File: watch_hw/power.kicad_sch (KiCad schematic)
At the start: 21 parts, among them Q2 SSM6J501NU, U3 MAX17048G+, U4 LTC3130EUDC-1#PBF, U5 MCP73831-2ACI{slash}MC

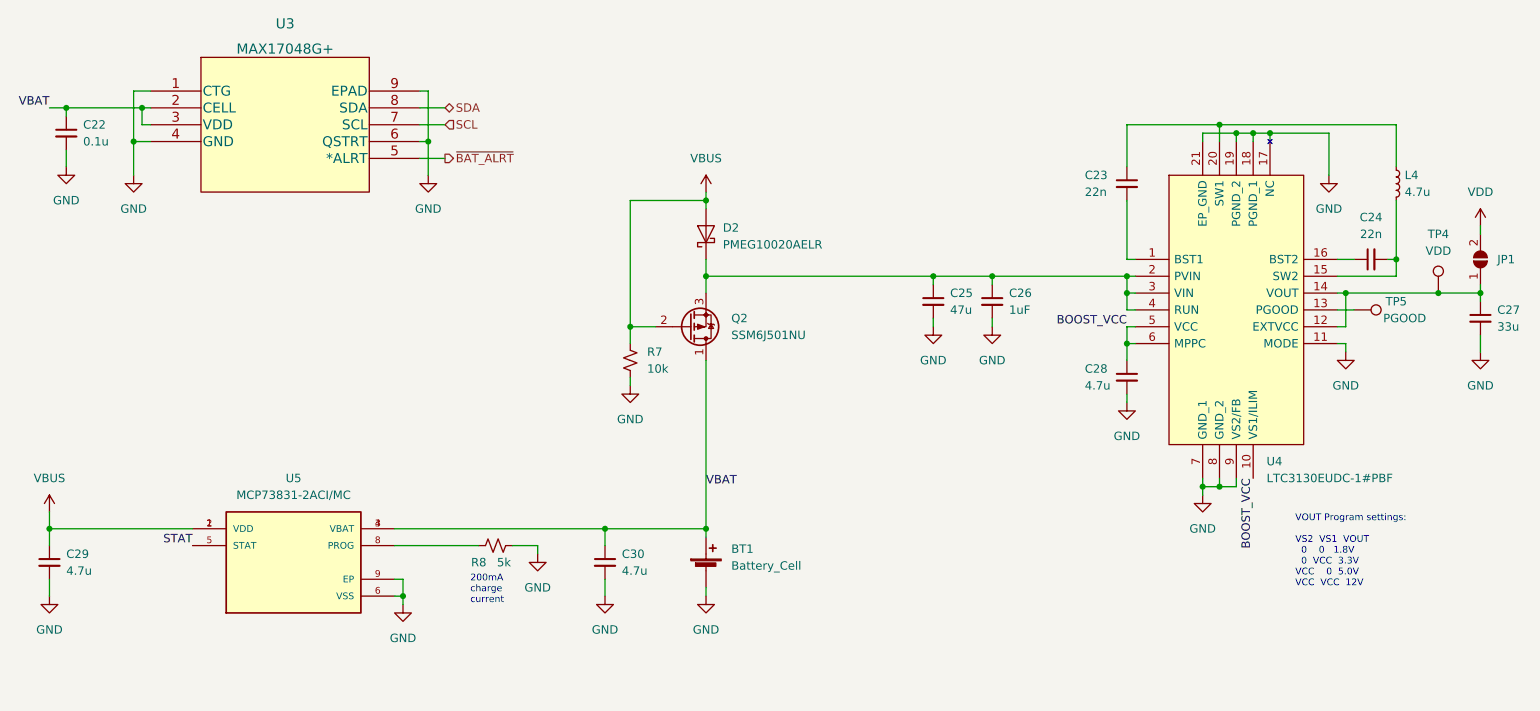
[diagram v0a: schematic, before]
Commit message: Finalize (?) part selection, start layout
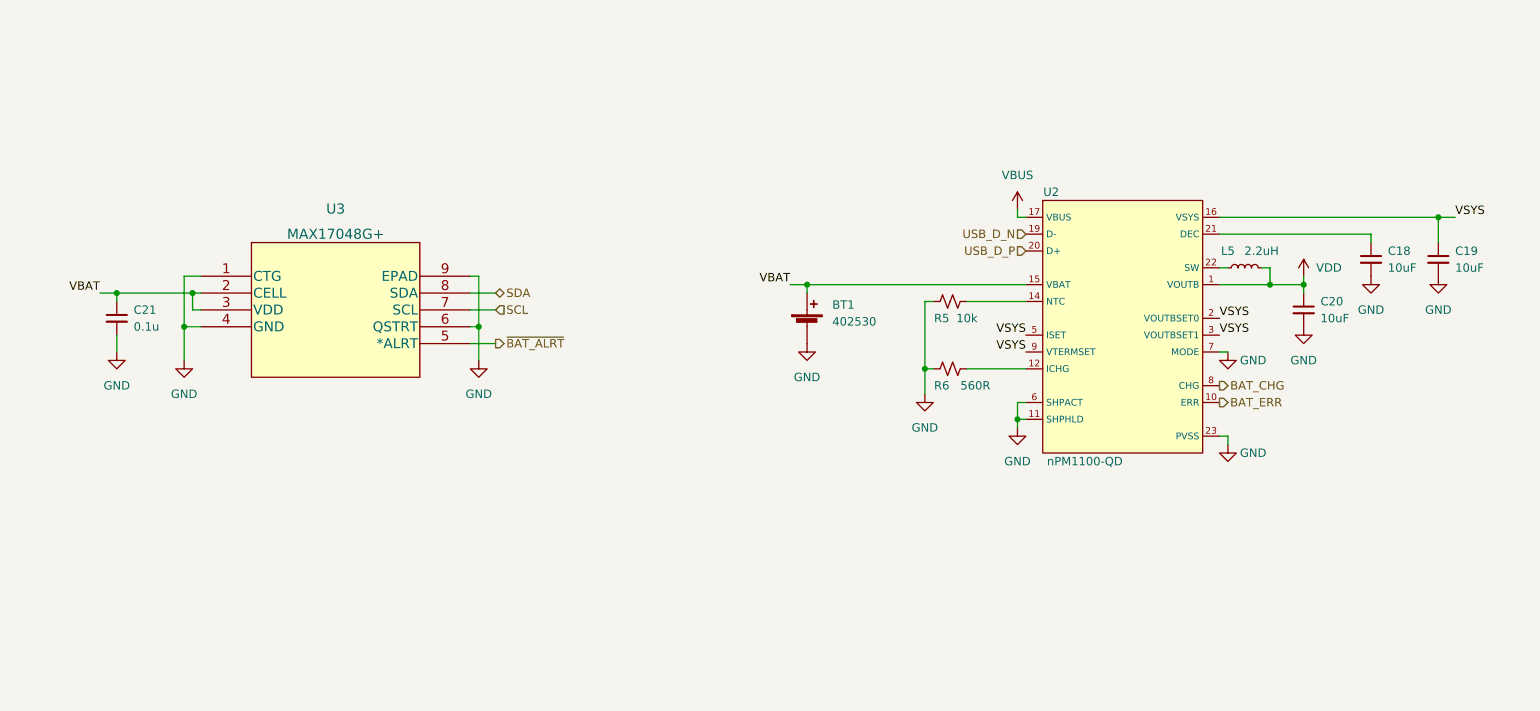
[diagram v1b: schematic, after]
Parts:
- removed C23, C24: 22n, Capacitor_SMD:C_0402_1005Metric_Pad0.74x0.62mm_HandSolder, symbol Device:C_Small
- removed C25: 47u, Capacitor_SMD:C_0402_1005Metric_Pad0.74x0.62mm_HandSolder, symbol Device:C_Small
- removed C26: 1uF, Capacitor_SMD:C_0402_1005Metric_Pad0.74x0.62mm_HandSolder, symbol Device:C_Small
- removed C27: 33u, Capacitor_SMD:C_0402_1005Metric_Pad0.74x0.62mm_HandSolder, symbol Device:C_Small
- removed C28, C29, C30: 4.7u, Capacitor_SMD:C_0402_1005Metric_Pad0.74x0.62mm_HandSolder, symbol Device:C_Small
- removed D2: PMEG10020AELR, Diode_SMD:Nexperia_CFP3_SOD-123W, symbol Diode:PMEG10020AELR
- removed JP1: SolderJumper_2_Open, Jumper:SolderJumper-2_P1.3mm_Open_RoundedPad1.0x1.5mm, symbol Jumper:SolderJumper_2_Open
- removed L4: 4.7u, Inductor_SMD:L_0805_2012Metric_Pad1.15x1.40mm_HandSolder, symbol Device:L_Small
- removed Q2: SSM6J501NU, watch:TRANS_SSM6J501NU,LF, symbol Device:Q_PMOS_DGS
- removed R7: 10k, Resistor_SMD:R_0402_1005Metric_Pad0.72x0.64mm_HandSolder, symbol Device:R_Small_US
- removed R8: 5k, Resistor_SMD:R_0402_1005Metric_Pad0.72x0.64mm_HandSolder, symbol Device:R_Small_US
- removed TP4: VDD, TestPoint:TestPoint_THTPad_D1.0mm_Drill0.5mm, symbol Connector:TestPoint
- removed TP5: PGOOD, TestPoint:TestPoint_THTPad_D1.0mm_Drill0.5mm, symbol Connector:TestPoint
- removed U4: LTC3130EUDC-1#PBF, watch:QFN50P300X400X80-21M-D, symbol watch:LTC3130EUDC-1#PBF
- removed U5: MCP73831-2ACI/MC, watch:SON50P200X300X100-9N, symbol watch:MCP73831-2ACI{brace}slash}MC
- added C18, C19, C20: 10uF, Capacitor_SMD:C_0805_2012Metric_Pad1.18x1.45mm_HandSolder, symbol Device:C_Small
- added L5: 2.2uH, Inductor_SMD:L_0805_2012Metric_Pad1.05x1.20mm_HandSolder, symbol Device:L_Small
- added R5: 10k, Resistor_SMD:R_0402_1005Metric_Pad0.72x0.64mm_HandSolder, symbol Device:R_Small_US
- added R6: 560R, Resistor_SMD:R_0402_1005Metric_Pad0.72x0.64mm_HandSolder, symbol Device:R_Small_US
- added U2: nPM1100-QD, watch:nPM1100-QD, symbol watch:nPM1100-QD
- BT1: value Battery_Cell -> 402530
- renumbered C22 to C21
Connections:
- net GND: now also C18.2, C19.2, C20.2, R5.1, R6.1, U2.11 (SHPHLD), U2.23 (PVSS), U2.6 (SHPACT), U2.7 (MODE)
- net VBAT: now also U2.15 (VBAT)
- net VBUS: now also U2.17 (VBUS)
- net VDD: now also C20.1, L5.2, U2.1 (VOUTB)
- new net: L5.1, U2.22 (SW)
- new net: C18.1, U2.21 (DEC)
- new net: R5.2, U2.14 (NTC)
- new net: R6.2, U2.12 (ICHG)
- new net BAT_CHG: U2.8 (CHG)
- new net BAT_ERR: U2.10 (ERR)
- new net USB_D_N: U2.19 (D-)
- new net USB_D_P: U2.20 (D+)
- new net VSYS: C19.1, U2.16 (VSYS), U2.2 (VOUTBSET0), U2.3 (VOUTBSET1), U2.5 (ISET), U2.9 (VTERMSET)
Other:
- note removed: "200mA charge current"
- note removed: "VOUT Program settings: VS2 VS1 VOUT 0 0 1.8V 0 VCC 3.3V VCC 0 5.0V VCC VCC 12V"
- moved on the sheet: BT1, C21, U3

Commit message: Clean up library symbols, update to kicad 8
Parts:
- C21: value 0.1u -> 0.1uF

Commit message: Start watch v1 layout
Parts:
- added TP1, TP2, TP3, TP4: TestPoint, TestPoint:TestPoint_Keystone_5015_Micro_Mini, symbol Connector:TestPoint
- U2: footprint watch:nPM1100-QD -> Package_DFN_QFN:QFN-24-1EP_4x4mm_P0.5mm_EP2.5x2.5mm
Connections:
- net GND: now also TP1.1
- net VBAT: now also TP3.1
- net VDD: now also TP2.1
- net VSYS: now also TP4.1

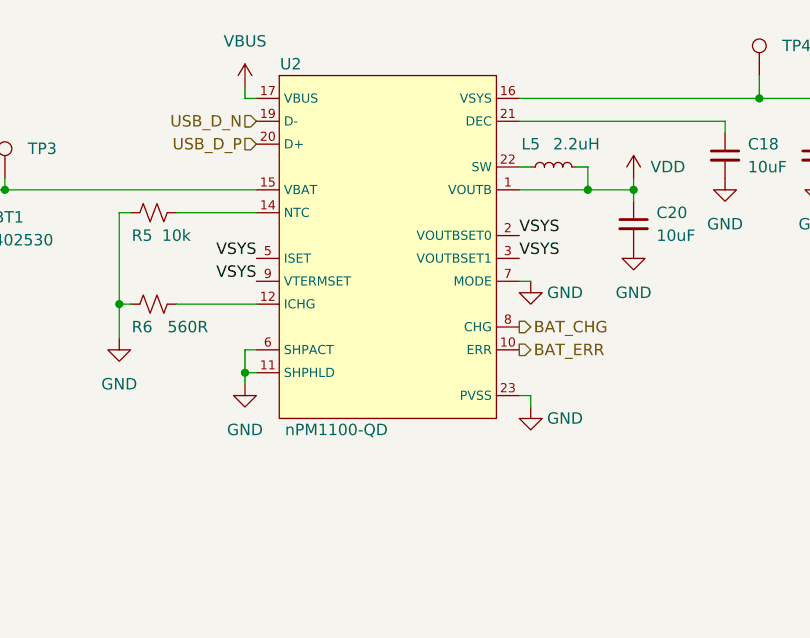
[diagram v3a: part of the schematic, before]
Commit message: Add pulse sensor straight to board, fix NPM1100 symbol/footprint
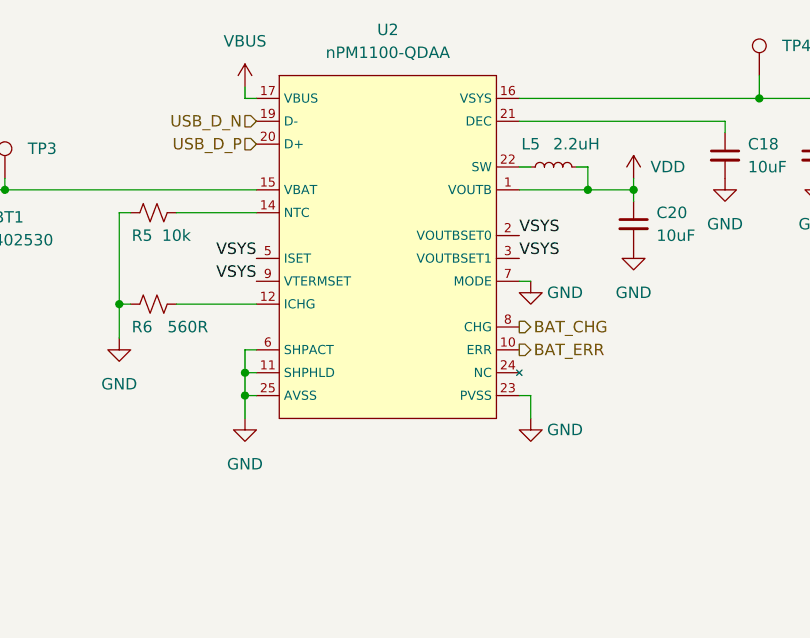
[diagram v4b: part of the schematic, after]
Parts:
- removed U2: nPM1100-QD, Package_DFN_QFN:QFN-24-1EP_4x4mm_P0.5mm_EP2.5x2.5mm, symbol watch:nPM1100-QD
- added U2: nPM1100-QDAA, Package_DFN_QFN:QFN-24-1EP_4x4mm_P0.5mm_EP2.15x2.15mm, symbol watch:nPM1100-QDAA
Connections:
- net BAT_CHG: now also U2.8 (CHG)
- net BAT_ERR: now also U2.10 (ERR)
- net GND: now also U2.11 (SHPHLD), U2.23 (PVSS), U2.25 (AVSS), U2.6 (SHPACT), U2.7 (MODE)
- net USB_D_N: now also U2.19 (D-)
- net USB_D_P: now also U2.20 (D+)
- net VBAT: now also U2.15 (VBAT)
- net VBUS: now also U2.17 (VBUS)
- net VDD: now also U2.1 (VOUTB)
- net VSYS: now also U2.16 (VSYS), U2.2 (VOUTBSET0), U2.3 (VOUTBSET1), U2.5 (ISET), U2.9 (VTERMSET)
- net at L5.1: now also U2.22 (SW)
- net at C18.1: now also U2.21 (DEC)
- net at R5.2: now also U2.14 (NTC)
- net at R6.2: now also U2.12 (ICHG)
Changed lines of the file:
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@@
+	)
+	(junction
+		(at 185.42 106.68)
+		(diameter 0)
+		(color 0 0 0 0)
 	)
 	(junction
@@
 	(wire
 		(pts
+			(xy 185.42 106.68) (xy 186.69 106.68)
+		)
+		(stroke
+			(width 0)
+			(type default)
+		)
+	)
+	(wire
+		(pts
 			(xy 158.75 83.82) (xy 186.69 83.82)
 		)
@@
 	(wire
 		(pts
-			(xy 185.42 105.41) (xy 185.42 104.14)
+			(xy 185.42 109.22) (xy 185.42 106.68)
 		)
 		(stroke
@@
 	(wire
 		(pts
+			(xy 185.42 106.68) (xy 185.42 104.14)
+		)
+		(stroke
+			(width 0)
+			(type default)
+		)
+	)
+	(wire
+		(pts
 			(xy 185.42 72.39) (xy 185.42 73.66)
 		)
@@
 	(wire
 		(pts
-			(xy 217.17 107.95) (xy 217.17 106.68)
+			(xy 217.17 109.22) (xy 217.17 106.68)
 		)
 		(stroke
@@
 	)
 	(symbol
+		(lib_id "watch:nPM1100-QDAA")
+		(at 186.69 73.66 0)
+		(unit 1)
+		(exclude_from_sim no)
+		(in_bom yes)
+		(on_board yes)
+		(dnp no)
+		(fields_autoplaced yes)
+		(property "Reference" "U2"
+			(at 201.295 66.04 0)
+			(effects
+				(font
+					(size 1.27 1.27)
+				)
+			)
+		)
+		(property "Value" "nPM1100-QDAA"
+			(at 201.295 68.58 0)
+			(effects
+				(font
+					(size 1.27 1.27)
+				)
+			)
+		)
+		(property "Footprint" "Package_DFN_QFN:QFN-24-1EP_4x4mm_P0.5mm_EP2.15x2.15mm"
+			(at 199.39 64.77 0)
+			(effects
+				(font
+					(size 1.27 1.27)
+				)
+				(hide yes)
+			)
+		)
+		(property "Datasheet" "https://infocenter.nordicsemi.com/pdf/nPM1100_PS_v1.3.pdf"
+			(at 187.96 73.66 0)
+			(effects
+				(font
+					(size 1.27 1.27)
+				)
+				(hide yes)
+			)
+		)
+		(property "Description" "POWER MANAGEMENT IC QFN24 VTERM"
+			(at 186.69 73.66 0)
+			(effects
+				(font
+					(size 1.27 1.27)
+				)
+				(hide yes)
+			)
+		)
+		(property "Manufacturer" "Nordic Semiconductor"
+			(at 186.69 73.66 0)
+			(effects
+				(font
+					(size 1.27 1.27)
+				)
+				(hide yes)
+			)
+		)
+		(pin "17"
+		)
+		(pin "8"
+		)
+		(pin "15"
+		)
+		(pin "22"
+		)
+		(pin "16"
+		)
+		(pin "14"
+		)
+		(pin "5"
+		)
+		(pin "18"
+		)
+		(pin "25"
+		)
+		(pin "21"
+		)
+		(pin "11"
+		)
+		(pin "1"
+		)
+		(pin "6"
+		)
+		(pin "24"
+		)
+		(pin "20"
+		)
+		(pin "12"
+		)
+		(pin "4"
+		)
+		(pin "13"
+		)
+		(pin "19"
+		)
+		(pin "2"
+		)
+		(pin "9"
+		)
+		(pin "3"
+		)
+		(pin "7"
+		)
+		(pin "23"
+		)
+		(pin "10"
+		)
+		(instances
+			(project ""
+				(path "/7f737de8-b7e5-4967-9e9f-b541c91fc2b3/2145fa36-acde-4973-ae1a-fee76383e6bf"
+					(reference "U2")
+					(unit 1)
+				)
+			)
+		)
+	)
+	(symbol
 		(lib_id "Device:L_Small")
 		(at 219.71 81.28 90)
@@
 		(lib_name "GND_1")
 		(lib_id "power:GND")
-		(at 185.42 105.41 0)
+		(at 185.42 109.22 0)
 		(unit 1)
 		(exclude_from_sim no)
@@
 		(fields_autoplaced yes)
 		(property "Reference" "#PWR043"
-			(at 185.42 111.76 0)
+			(at 185.42 115.57 0)
 			(effects
 				(font
@@
 		)
 		(property "Value" "GND"
-			(at 185.42 110.49 0)
+			(at 185.42 114.3 0)
 			(effects
 				(font
@@
 		)
 		(property "Footprint" ""
-			(at 185.42 105.41 0)
+			(at 185.42 109.22 0)
 			(effects
 				(font
@@
 		)
 		(property "Datasheet" ""
-			(at 185.42 105.41 0)
+			(at 185.42 109.22 0)
 			(effects
 				(font
@@
 		)
 		(property "Description" ""
-			(at 185.42 105.41 0)
+			(at 185.42 109.22 0)
 			(effects
 				(font
@@
 		(lib_name "GND_1")
 		(lib_id "power:GND")
-		(at 217.17 107.95 0)
+		(at 217.17 109.22 0)
 		(unit 1)
 		(exclude_from_sim no)
@@
 		(dnp no)
 		(property "Reference" "#PWR044"
-			(at 217.17 114.3 0)
+			(at 217.17 115.57 0)
 			(effects
 				(font
@@
 		)
 		(property "Value" "GND"
-			(at 220.98 109.22 0)
+			(at 220.98 110.49 0)
 			(effects
 				(font
@@
 		)
 		(property "Footprint" ""
-			(at 217.17 107.95 0)
+			(at 217.17 109.22 0)
 			(effects
 				(font
@@
 		)
 		(property "Datasheet" ""
-			(at 217.17 107.95 0)
+			(at 217.17 109.22 0)
 			(effects
 				(font
@@
 		)
 		(property "Description" ""
-			(at 217.17 107.95 0)
+			(at 217.17 109.22 0)
 			(effects
 				(font
@@
 					(unit 1)
 				)
-			)
-		)
-	)
-	(symbol
-		(lib_id "watch:nPM1100-QD")
-		(at 186.69 73.66 0)
-		(unit 1)
-		(exclude_from_sim no)
-		(in_bom yes)
-		(on_board yes)
-		(dnp no)
-		(property "Reference" "U2"
-			(at 190.5 69.85 0)
-			(effects
-				(font
-					(size 1.27 1.27)
-				)
-			)
-		)
-		(property "Value" "nPM1100-QD"
-			(at 195.58 110.49 0)
-			(effects
-				(font
-					(size 1.27 1.27)
-				)
-			)
-		)
-		(property "Footprint" "Package_DFN_QFN:QFN-24-1EP_4x4mm_P0.5mm_EP2.5x2.5mm"
-			(at 187.96 73.66 0)
-			(effects
-				(font
-					(size 1.27 1.27)
-				)
-				(hide yes)
-			)
-		)
-		(property "Datasheet" "https://docs-be.nordicsemi.com/bundle/ps_npm1100/page/nPM1100_PS_v1.5.pdf?_LANG=enus"
-			(at 187.96 73.66 0)
-			(effects
-				(font
-					(size 1.27 1.27)
-				)
-				(hide yes)
-			)
-		)
-		(property "Description" ""
-			(at 186.69 73.66 0)
-			(effects
-				(font
-					(size 1.27 1.27)
-				)
-				(hide yes)
-			)
-		)
-		(pin "1"
-		)
-		(pin "10"
-		)
-		(pin "11"
-		)
-		(pin "12"
-		)
-		(pin "13"
-		)
-		(pin "14"
-		)
-		(pin "15"
-		)
-		(pin "16"
-		)
-		(pin "17"
-		)
-		(pin "18"
-		)
-		(pin "19"
-		)
-		(pin "2"
-		)
-		(pin "20"
-		)
-		(pin "21"
-		)
-		(pin "22"
-		)
-		(pin "23"
-		)
-		(pin "3"
-		)
-		(pin "4"
-		)
-		(pin "5"
-		)
-		(pin "6"
-		)
-		(pin "7"
-		)
-		(pin "8"
-		)
-		(pin "9"
-		)
-		(instances
-			(project "watch"
-				(path "/7f737de8-b7e5-4967-9e9f-b541c91fc2b3/2145fa36-acde-4973-ae1a-fee76383e6bf"
-					(reference "U2")
-					(unit 1)
-				)

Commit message: finish routing, need to fix DRC
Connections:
- net USB_D_N is gone; now on net GND: U2.19 (D-)
- net USB_D_P: no longer names the net of U2.20 (D+)
- no-connect marks 0 -> 1
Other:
- note added: "Charge current limit = 300mA R_ICHG = 625 / ICHG - 1562.5"
- note added: "VBUS current limit = 500mA ISET = VSYS D- = AVSS D+ = NC"
- moved on the sheet: R5, R6
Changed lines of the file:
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@@
 	(generator_version "9.0")
 	(paper "A4")
+	(text "Charge current limit = 300mA\nR_ICHG = 625 / ICHG - 1562.5"
+		(exclude_from_sim no)
+		(at 146.304 111.506 0)
+		(effects
+			(font
+				(size 1.27 1.27)
+			)
+			(justify left)
+		)
+	)
+	(text "VBUS current limit = 500mA\nISET = VSYS\nD- = AVSS\nD+ = NC"
+		(exclude_from_sim no)
+		(at 157.988 60.452 0)
+		(effects
+			(font
+				(size 1.27 1.27)
+			)
+			(justify left)
+		)
+	)
+	(junction
+		(at 185.42 101.6)
+		(diameter 0)
+		(color 0 0 0 0)
+	)
 	(junction
 		(at 242.57 73.66)
@@
 	)
 	(junction
-		(at 171.45 96.52)
+		(at 166.37 96.52)
 		(diameter 0)
 		(color 0 0 0 0)
 	)
+	(no_connect
+		(at 186.69 78.74)
+	)
 	(wire
 		(pts
@@
 	(wire
 		(pts
+			(xy 185.42 76.2) (xy 185.42 101.6)
+		)
+		(stroke
+			(width 0)
+			(type default)
+		)
+	)
+	(wire
+		(pts
 			(xy 102.87 82.55) (xy 104.14 82.55)
 		)
@@
 	(wire
 		(pts
+			(xy 181.61 93.98) (xy 186.69 93.98)
+		)
+		(stroke
+			(width 0)
+			(type default)
+		)
+	)
+	(wire
+		(pts
 			(xy 60.96 85.09) (xy 60.96 87.63)
 		)
@@
 	(wire
 		(pts
-			(xy 171.45 96.52) (xy 171.45 100.33)
+			(xy 166.37 96.52) (xy 166.37 100.33)
 		)
 		(stroke
@@
 	(wire
 		(pts
+			(xy 181.61 91.44) (xy 186.69 91.44)
+		)
+		(stroke
+			(width 0)
+			(type default)
+		)
+	)
+	(wire
+		(pts
 			(xy 59.69 82.55) (xy 62.23 82.55)
 		)
@@
 	(wire
 		(pts
-			(xy 171.45 96.52) (xy 172.72 96.52)
+			(xy 166.37 96.52) (xy 167.64 96.52)
 		)
 		(stroke
@@
 	(wire
 		(pts
+			(xy 186.69 76.2) (xy 185.42 76.2)
+		)
+		(stroke
+			(width 0)
+			(type default)
+		)
+	)
+	(wire
+		(pts
 			(xy 104.14 90.17) (xy 102.87 90.17)
 		)
@@
 	(wire
 		(pts
-			(xy 177.8 96.52) (xy 186.69 96.52)
-		)
-		(stroke
-			(width 0)
-			(type default)
-		)
-	)
-	(wire
-		(pts
-			(xy 171.45 86.36) (xy 171.45 96.52)
+			(xy 172.72 96.52) (xy 186.69 96.52)
+		)
+		(stroke
+			(width 0)
+			(type default)
+		)
+	)
+	(wire
+		(pts
+			(xy 166.37 86.36) (xy 166.37 96.52)
 		)
 		(stroke
@@
 	(wire
 		(pts
-			(xy 172.72 86.36) (xy 171.45 86.36)
+			(xy 167.64 86.36) (xy 166.37 86.36)
 		)
 		(stroke
@@
 	(wire
 		(pts
-			(xy 177.8 86.36) (xy 186.69 86.36)
+			(xy 172.72 86.36) (xy 186.69 86.36)
 		)
 		(stroke
@@
 	)
 	(label "VSYS"
-		(at 186.69 91.44 180)
+		(at 181.61 91.44 180)
 		(effects
 			(font
@@
 	)
 	(label "VSYS"
-		(at 186.69 93.98 180)
+		(at 181.61 93.98 180)
 		(effects
 			(font
@@
 		)
 	)
-	(hierarchical_label "USB_D_P"
-		(shape input)
-		(at 186.69 78.74 180)
-		(effects
-			(font
-				(size 1.27 1.27)
-			)
-			(justify right)
-		)
-	)
-	(hierarchical_label "USB_D_N"
-		(shape input)
-		(at 186.69 76.2 180)
-		(effects
-			(font
-				(size 1.27 1.27)
-			)
-			(justify right)
-		)
-	)
 	(symbol
 		(lib_id "power:VBUS")
@@
 		(lib_name "GND_1")
 		(lib_id "power:GND")
-		(at 171.45 100.33 0)
+		(at 166.37 100.33 0)
 		(unit 1)
 		(exclude_from_sim no)
@@
 		(fields_autoplaced yes)
 		(property "Reference" "#PWR042"
-			(at 171.45 106.68 0)
+			(at 166.37 106.68 0)
 			(effects
 				(font
@@
 		)
 		(property "Value" "GND"
-			(at 171.45 105.41 0)
+			(at 166.37 105.41 0)
 			(effects
 				(font
@@
 		)
 		(property "Footprint" ""
-			(at 171.45 100.33 0)
+			(at 166.37 100.33 0)
 			(effects
 				(font
@@
 		)
 		(property "Datasheet" ""
-			(at 171.45 100.33 0)
+			(at 166.37 100.33 0)
 			(effects
 				(font
@@
 		)
 		(property "Description" ""
-			(at 171.45 100.33 0)
+			(at 166.37 100.33 0)
 			(effects
 				(font
@@
 			)
 		)
-		(property "Datasheet" "https://infocenter.nordicsemi.com/pdf/nPM1100_PS_v1.3.pdf"
+		(property "Datasheet" "https://docs-be.nordicsemi.com/bundle/ps_npm1100/page/nPM1100_PS_v1.5.pdf"
 			(at 187.96 73.66 0)
 			(effects
@@
 	(symbol
 		(lib_id "Device:R_Small_US")
-		(at 175.26 86.36 90)
+		(at 170.18 86.36 90)
 		(unit 1)
 		(exclude_from_sim no)
@@
 		(dnp no)
 		(property "Reference" "R5"
-			(at 173.99 88.9 90)
+			(at 168.91 88.9 90)
 			(effects
 				(font
@@
 		)
 		(property "Value" "10k"
-			(at 177.8 88.9 90)
+			(at 172.72 88.9 90)
 			(effects
 				(font
@@
 		)
 		(property "Footprint" "Resistor_SMD:R_0402_1005Metric_Pad0.72x0.64mm_HandSolder"
-			(at 175.26 86.36 0)
+			(at 170.18 86.36 0)
 			(effects
 				(font
@@
 		)
 		(property "Datasheet" "~"
-			(at 175.26 86.36 0)
+			(at 170.18 86.36 0)
 			(effects
 				(font
@@
 		)
 		(property "Description" ""
-			(at 175.26 86.36 0)
+			(at 170.18 86.36 0)
 			(effects
 				(font
@@
 	(symbol
 		(lib_id "Device:R_Small_US")
-		(at 175.26 96.52 90)
+		(at 170.18 96.52 90)
 		(unit 1)
 		(exclude_from_sim no)
@@
 		(dnp no)
 		(property "Reference" "R6"
+			(at 168.91 99.06 90)
+			(effects
+				(font
+					(size 1.27 1.27)
+				)
+			)
+		)
+		(property "Value" "560R"
 			(at 173.99 99.06 90)
 			(effects
@@
 			)
 		)
-		(property "Value" "560R"
-			(at 179.07 99.06 90)
-			(effects
-				(font
-					(size 1.27 1.27)
-				)
-			)
-		)
 		(property "Footprint" "Resistor_SMD:R_0402_1005Metric_Pad0.72x0.64mm_HandSolder"
-			(at 175.26 96.52 0)
+			(at 170.18 96.52 0)
 			(effects
 				(font
@@
 		)
 		(property "Datasheet" "~"
-			(at 175.26 96.52 0)
+			(at 170.18 96.52 0)
 			(effects
 				(font
@@
 		)
 		(property "Description" ""
-			(at 175.26 96.52 0)
-			(effects
-				(font
+			(at 170.18 96.52 0)
+			(effects
+				(font
